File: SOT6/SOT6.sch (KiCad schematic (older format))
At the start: 3 parts, among them J1 Conn_01x03, J2 Conn_01x03, J3 Conn_02x03_Counter_Clockwise

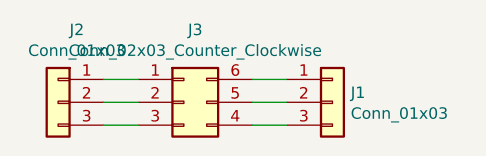
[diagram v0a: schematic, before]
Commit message: Silkscreens and sizes updated
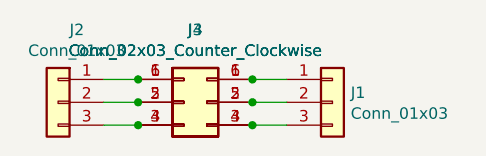
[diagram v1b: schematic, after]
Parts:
- added J4: Conn_02x03_Counter_Clockwise, Package_TO_SOT_SMD:SOT-363_SC-70-6, symbol Connector_Generic:Conn_02x03_Counter_Clockwise
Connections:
- net at J1.1 (Pin_1), J3.6 (Pin_6): now also J4.1 (Pin_1)
- net at J1.2 (Pin_2), J3.5 (Pin_5): now also J4.2 (Pin_2)
- net at J1.3 (Pin_3), J3.4 (Pin_4): now also J4.3 (Pin_3)
- net at J2.1 (Pin_1), J3.1 (Pin_1): now also J4.6 (Pin_6)
- net at J2.2 (Pin_2), J3.2 (Pin_2): now also J4.5 (Pin_5)
- net at J2.3 (Pin_3), J3.3 (Pin_3): now also J4.4 (Pin_4)
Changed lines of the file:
@@
 EESchema Schematic File Version 4
+LIBS:SOT6-cache
 EELAYER 29 0
 EELAYER END
@@
 Wire Wire Line
 	4850 3600 5000 3600
+$Comp
+L Connector_Generic:Conn_02x03_Counter_Clockwise J4
+U 1 1 5D3AAC75
+P 4650 3500
+F 0 "J4" H 4700 3817 50  0000 C CNN
+F 1 "Conn_02x03_Counter_Clockwise" H 4700 3726 50  0000 C CNN
+F 2 "Package_TO_SOT_SMD:SOT-363_SC-70-6" H 4650 3500 50  0001 C CNN
+F 3 "~" H 4650 3500 50  0001 C CNN
+	1    4650 3500
+	-1   0    0    -1
+$EndComp
+Connection ~ 4350 3400
+Connection ~ 4350 3500
+Connection ~ 4350 3600
+Connection ~ 4850 3400
+Connection ~ 4850 3500
+Connection ~ 4850 3600
 $EndSCHEMATC

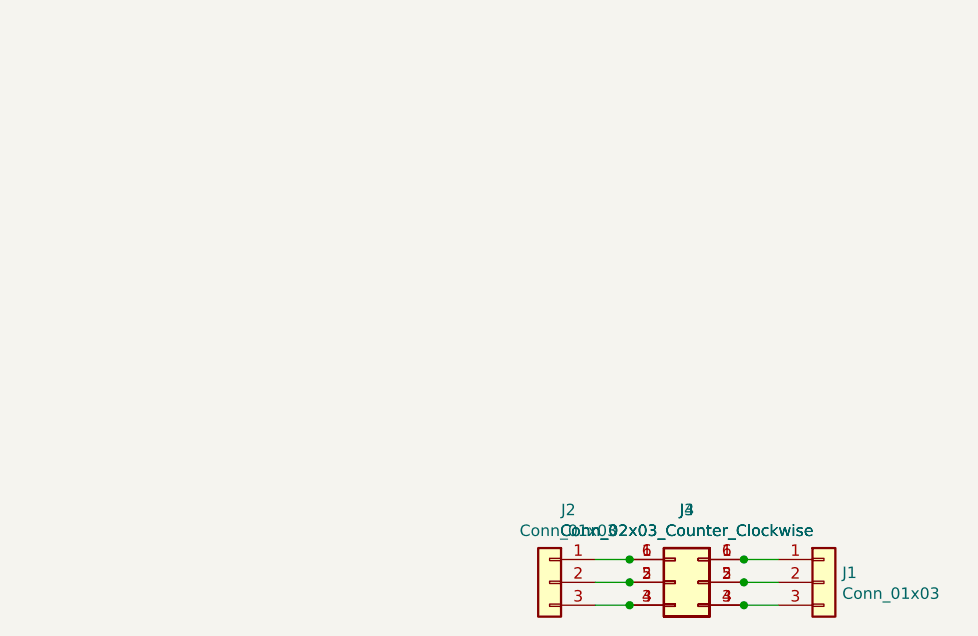
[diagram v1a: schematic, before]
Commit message: USB, SD and CR Cells Added
MicroSD, MicroUSB, MiniUSB, USB-C, CR1220, CR2032 added as well as all schematics page sizes optimised
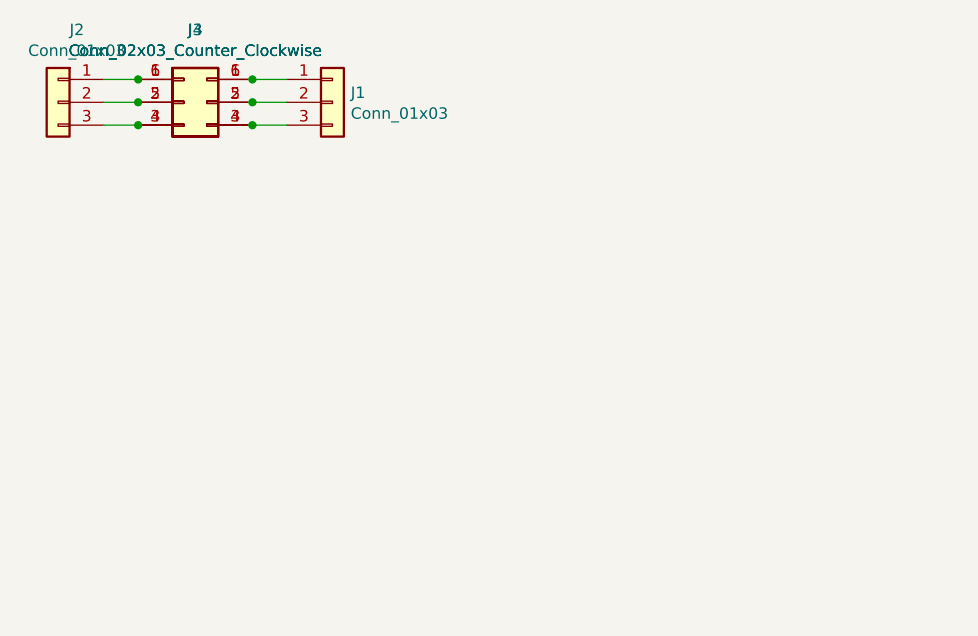
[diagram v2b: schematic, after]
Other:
- moved on the sheet: J1, J2, J3, J4
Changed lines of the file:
@@
 EELAYER 29 0
 EELAYER END
-$Descr A4 11693 8268
+$Descr User 5197 4016
 encoding utf-8
 Sheet 1 1
-Title ""
-Date ""
-Rev ""
-Comp ""
-Comment1 ""
-Comment2 ""
-Comment3 ""
+Title "SOT23 to DIP Breakout Board"
+Date "2019-07-04"
+Rev "1"
+Comp "SirBoard"
+Comment1 "SOT23-6 P = 0.95mm"
+Comment2 "SC-70 P = 0.65mm"
+Comment3 "DIP6 P = 2.54mm"
 Comment4 ""
 $EndDescr
@@
 L Connector_Generic:Conn_01x03 J1
 U 1 1 5D1DC59C
-P 5200 3500
-F 0 "J1" H 5280 3542 50  0000 L CNN
-F 1 "Conn_01x03" H 5280 3451 50  0000 L CNN
-F 2 "Connector_PinHeader_2.54mm:PinHeader_1x03_P2.54mm_Vertical" H 5200 3500 50  0001 C CNN
-F 3 "~" H 5200 3500 50  0001 C CNN
-	1    5200 3500
+P 3050 1400
+F 0 "J1" H 3130 1442 50  0000 L CNN
+F 1 "Conn_01x03" H 3130 1351 50  0000 L CNN
+F 2 "Connector_PinHeader_2.54mm:PinHeader_1x03_P2.54mm_Vertical" H 3050 1400 50  0001 C CNN
+F 3 "~" H 3050 1400 50  0001 C CNN
+	1    3050 1400
 	1    0    0    -1
 $EndComp
@@
 L Connector_Generic:Conn_02x03_Counter_Clockwise J3
 U 1 1 5D1DC7E1
-P 4550 3500
-F 0 "J3" H 4600 3817 50  0000 C CNN
-F 1 "Conn_02x03_Counter_Clockwise" H 4600 3726 50  0000 C CNN
-F 2 "Package_TO_SOT_SMD:SOT-23-6_Handsoldering" H 4550 3500 50  0001 C CNN
-F 3 "~" H 4550 3500 50  0001 C CNN
-	1    4550 3500
+P 2400 1400
+F 0 "J3" H 2450 1717 50  0000 C CNN
+F 1 "Conn_02x03_Counter_Clockwise" H 2450 1626 50  0000 C CNN
+F 2 "Package_TO_SOT_SMD:SOT-23-6_Handsoldering" H 2400 1400 50  0001 C CNN
+F 3 "~" H 2400 1400 50  0001 C CNN
+	1    2400 1400
 	1    0    0    -1
 $EndComp
@@
 L Connector_Generic:Conn_01x03 J2
 U 1 1 5D1DD0C5
-P 4000 3500
-F 0 "J2" H 3918 3817 50  0000 C CNN
-F 1 "Conn_01x03" H 3918 3726 50  0000 C CNN
-F 2 "Connector_PinHeader_2.54mm:PinHeader_1x03_P2.54mm_Vertical" H 4000 3500 50  0001 C CNN
-F 3 "~" H 4000 3500 50  0001 C CNN
-	1    4000 3500
+P 1850 1400
+F 0 "J2" H 1768 1717 50  0000 C CNN
+F 1 "Conn_01x03" H 1768 1626 50  0000 C CNN
+F 2 "Connector_PinHeader_2.54mm:PinHeader_1x03_P2.54mm_Vertical" H 1850 1400 50  0001 C CNN
+F 3 "~" H 1850 1400 50  0001 C CNN
+	1    1850 1400
 	-1   0    0    -1
 $EndComp
 Wire Wire Line
-	4200 3400 4350 3400
+	2050 1300 2200 1300
 Wire Wire Line
-	4350 3500 4200 3500
+	2200 1400 2050 1400
 Wire Wire Line
-	4200 3600 4350 3600
+	2050 1500 2200 1500
 Wire Wire Line
-	4850 3400 5000 3400
+	2700 1300 2850 1300
 Wire Wire Line
-	5000 3500 4850 3500
+	2850 1400 2700 1400
 Wire Wire Line
-	4850 3600 5000 3600
+	2700 1500 2850 1500
 $Comp
 L Connector_Generic:Conn_02x03_Counter_Clockwise J4
 U 1 1 5D3AAC75
-P 4650 3500
-F 0 "J4" H 4700 3817 50  0000 C CNN
-F 1 "Conn_02x03_Counter_Clockwise" H 4700 3726 50  0000 C CNN
-F 2 "Package_TO_SOT_SMD:SOT-363_SC-70-6" H 4650 3500 50  0001 C CNN
-F 3 "~" H 4650 3500 50  0001 C CNN
-	1    4650 3500
+P 2500 1400
+F 0 "J4" H 2550 1717 50  0000 C CNN
+F 1 "Conn_02x03_Counter_Clockwise" H 2550 1626 50  0000 C CNN
+F 2 "Package_TO_SOT_SMD:SOT-363_SC-70-6" H 2500 1400 50  0001 C CNN
+F 3 "~" H 2500 1400 50  0001 C CNN
+	1    2500 1400
 	-1   0    0    -1
 $EndComp
-Connection ~ 4350 3400
-Connection ~ 4350 3500
-Connection ~ 4350 3600
-Connection ~ 4850 3400
-Connection ~ 4850 3500
-Connection ~ 4850 3600
+Connection ~ 2200 1300
+Connection ~ 2200 1400
+Connection ~ 2200 1500
+Connection ~ 2700 1300
+Connection ~ 2700 1400
+Connection ~ 2700 1500
 $EndSCHEMATC
